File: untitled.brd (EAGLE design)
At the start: 59.4 x 57.8 mm, 21 parts

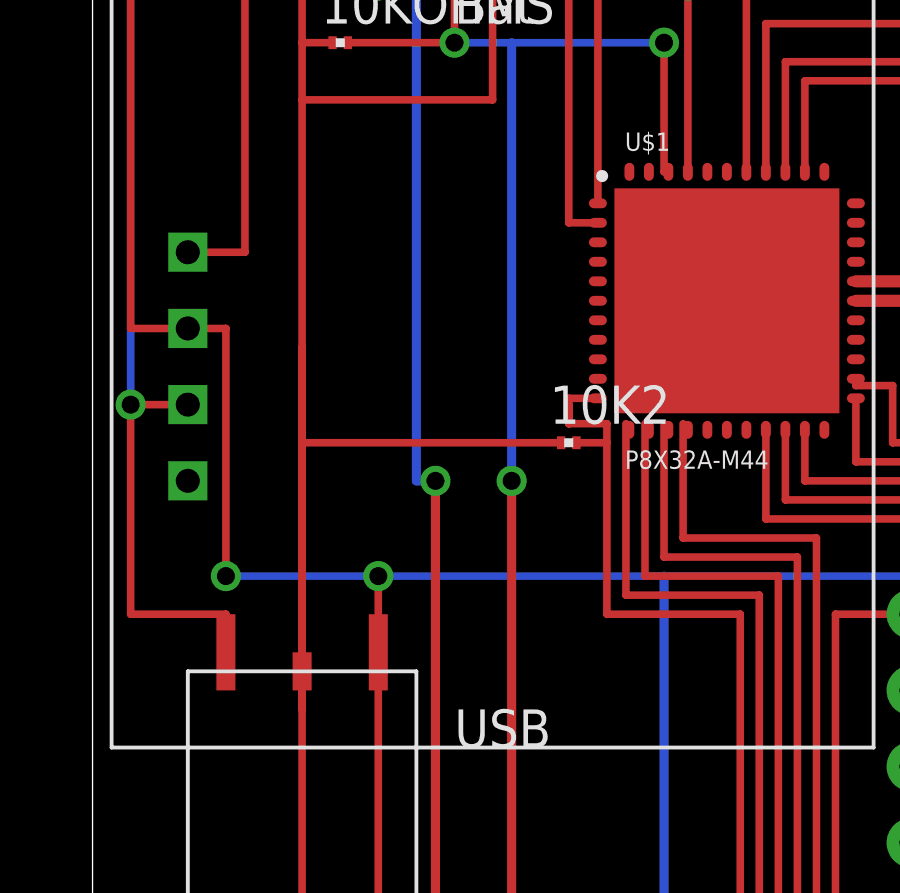
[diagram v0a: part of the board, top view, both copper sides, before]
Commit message: added power pins
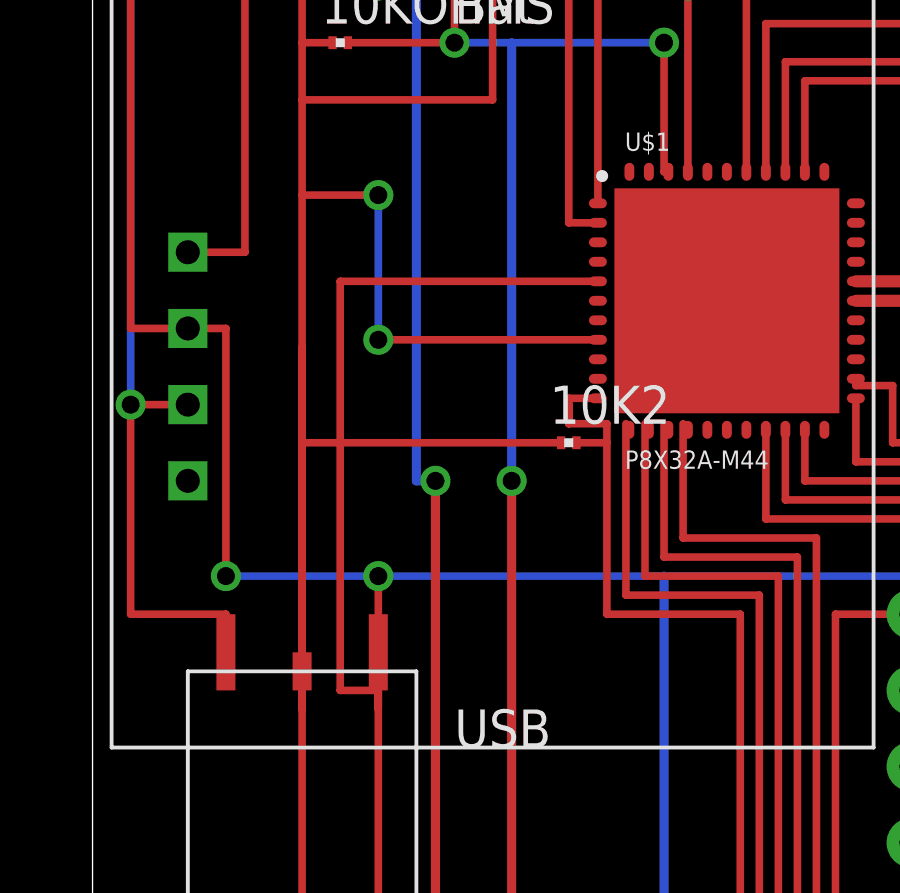
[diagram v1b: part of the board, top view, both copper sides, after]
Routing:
- net VSS: track 0.00 -> 24.1 mm
- net VDD: track 0.00 -> 14.7 mm, vias 0 -> 2
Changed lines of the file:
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@@
 <contactref element="U$1" pad="30"/>
 <contactref element="U$1" pad="40"/>
-<wire x1="55.45" y1="38.5313" x2="50.5" y2="41.5313" width="0" layer="19" extent="1-1"/>
 <wire x1="59.1" y1="44.1313" x2="55.45" y2="38.5313" width="0" layer="19" extent="1-1"/>
 <wire x1="54.15" y1="47.1313" x2="59.1" y2="44.1313" width="0" layer="19" extent="1-1"/>
+<wire x1="50.5" y1="41.5313" x2="43.18" y2="41.5313" width="0.254" layer="1"/>
+<wire x1="43.18" y1="41.5313" x2="43.18" y2="46.355" width="0.254" layer="16"/>
+<wire x1="43.18" y1="46.355" x2="40.64" y2="46.355" width="0.254" layer="1"/>
+<wire x1="40.64" y1="46.355" x2="54.15" y2="47.1313" width="0" layer="19" extent="1-16"/>
+<via x="43.18" y="41.5313" extent="1-16" drill="0.6" shape="square"/>
+<via x="43.18" y="46.355" extent="1-16" drill="0.6" shape="square"/>
 </signal>
 <signal name="VSS">
@@
 <contactref element="U$1" pad="27"/>
 <contactref element="U$1" pad="39"/>
-<wire x1="54.8" y1="47.1313" x2="50.5" y2="43.4813" width="0" layer="19" extent="1-1"/>
 <wire x1="54.8" y1="38.5313" x2="50.5" y2="43.4813" width="0" layer="19" extent="1-1"/>
 <wire x1="59.1" y1="42.1813" x2="54.8" y2="38.5313" width="0" layer="19" extent="1-1"/>
+<wire x1="50.5" y1="43.4813" x2="41.91" y2="43.4813" width="0.254" layer="1"/>
+<wire x1="41.91" y1="43.4813" x2="41.91" y2="29.845" width="0.254" layer="1"/>
+<wire x1="41.91" y1="29.845" x2="43.18" y2="29.845" width="0.254" layer="1"/>
+<wire x1="43.18" y1="29.845" x2="43.18" y2="29.21" width="0.254" layer="1"/>
+<wire x1="43.18" y1="29.21" x2="54.8" y2="38.5313" width="0" layer="19" extent="1-16"/>
 </signal>
 <signal name="VBAT">

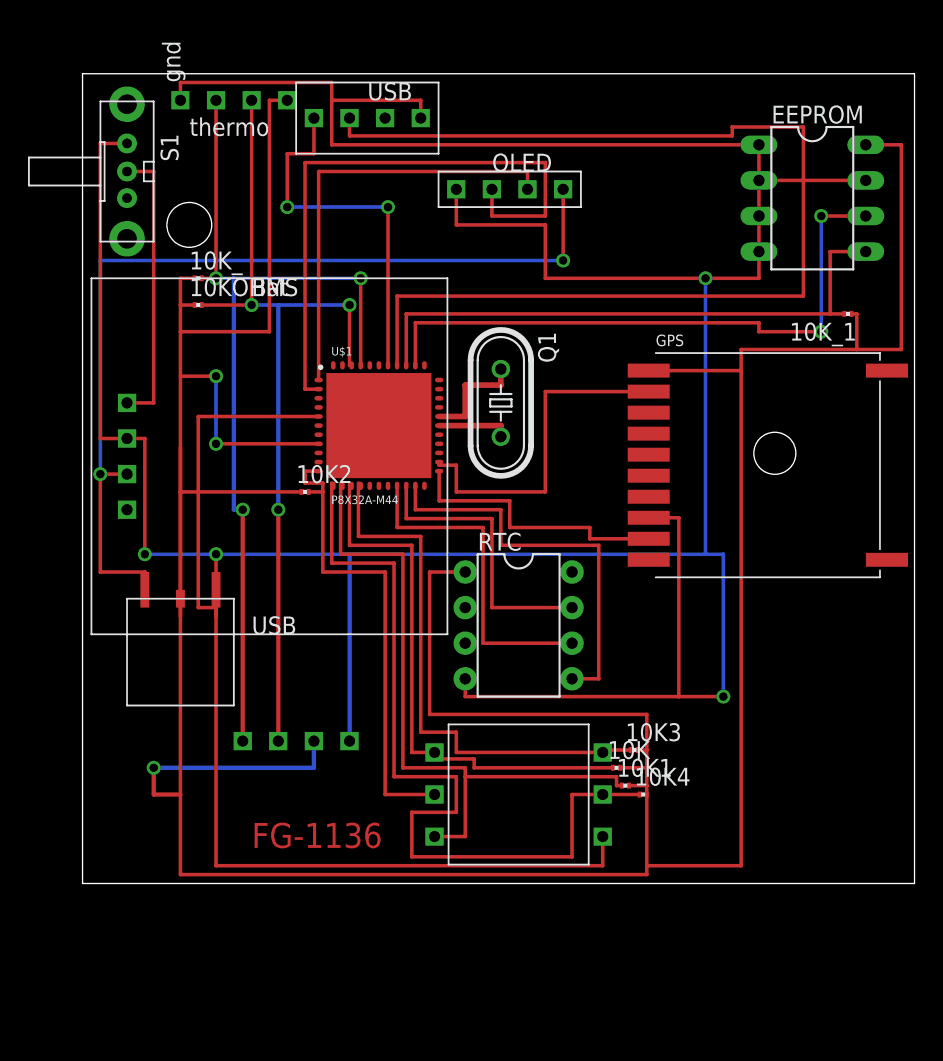
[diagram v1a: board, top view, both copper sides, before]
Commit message: used sane resistors
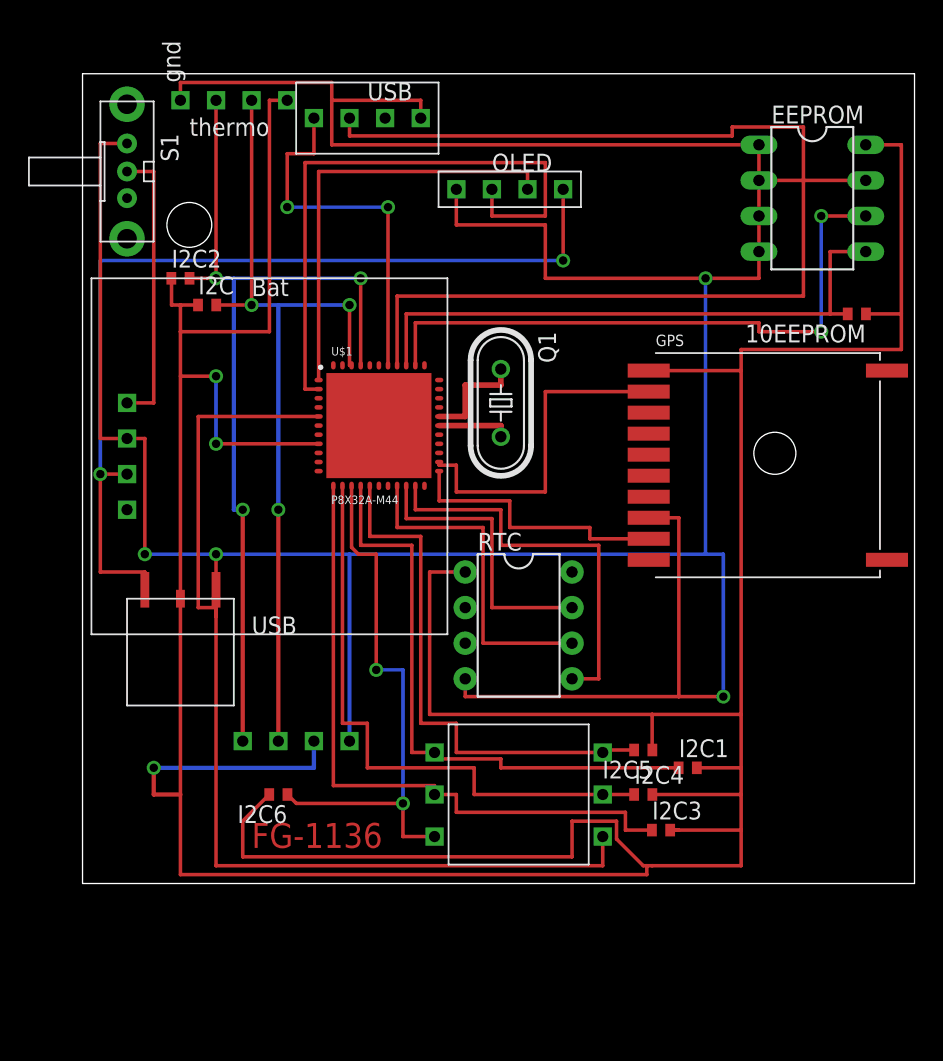
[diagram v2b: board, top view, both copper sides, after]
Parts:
- removed 10K, 10K1, 10K2, 10K3, 10K4, 10KOHMS, 10K_, 10K_1: (no value), rcl:R0201
- added 10EEPROM, I2C, I2C1, I2C2, I2C3, I2C4, I2C5, I2C6: (no value), adafruit:R1005
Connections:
- removed net N$22: 10K2.1, 5WAYSWITCH.U
- removed net N$23: 10K3.1, 5WAYSWITCH.BTN
- removed net N$24: 10K4.1, 5WAYSWITCH.R
- new net N$14: 5WAYSWITCH.U, I2C1.1, U$1.15
- new net N$15: 5WAYSWITCH.D, I2C6.1, U$1.14
- new net N$17: 5WAYSWITCH.L, I2C3.1, U$1.12
- net N$18: now also 10EEPROM.2; no longer 10K_1.2
- net N$20: now also 5WAYSWITCH.R, I2C4.1, U$1.13; no longer 10K.1, 5WAYSWITCH.D
- net N$21: now also 5WAYSWITCH.BTN, I2C5.2, U$1.16; no longer 10K1.1, 5WAYSWITCH.L
- net SCL: now also I2C2.2; no longer 10K_.2
- net SDA: now also I2C.2; no longer 10KOHMS.2
- net VCC: now also 10EEPROM.1, I2C.1, I2C1.2, I2C2.1, I2C3.2, I2C4.2, I2C5.1, I2C6.2; no longer 10K.2, 10K1.2, 10K2.2, 10K3.2, 10K4.2, 10KOHMS.1, 10K_.1, 10K_1.1, U$1.11, U$1.12, U$1.13, U$1.14, U$1.15
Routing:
- net N$24: track 59.4 -> 0.00 mm
- net N$17: track 0.00 -> 47.3 mm
- net N$22: track 46.0 -> 0.00 mm
- net VCC: track 247.0 -> 291.6 mm
- net N$14: track 0.00 -> 42.8 mm
- net N$15: track 0.00 -> 39.2 mm, vias 0 -> 2
- net N$23: track 38.8 -> 0.00 mm
- net N$20: track 50.7 -> 42.8 mm
- net N$21: track 43.9 -> 38.1 mm
- net SDA: track 60.7 -> 59.7 mm
- net SCL: track 63.9 -> 64.8 mm
- net N$16: track 0.00 -> 0.64 mm

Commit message: replaced compass break out with raw part
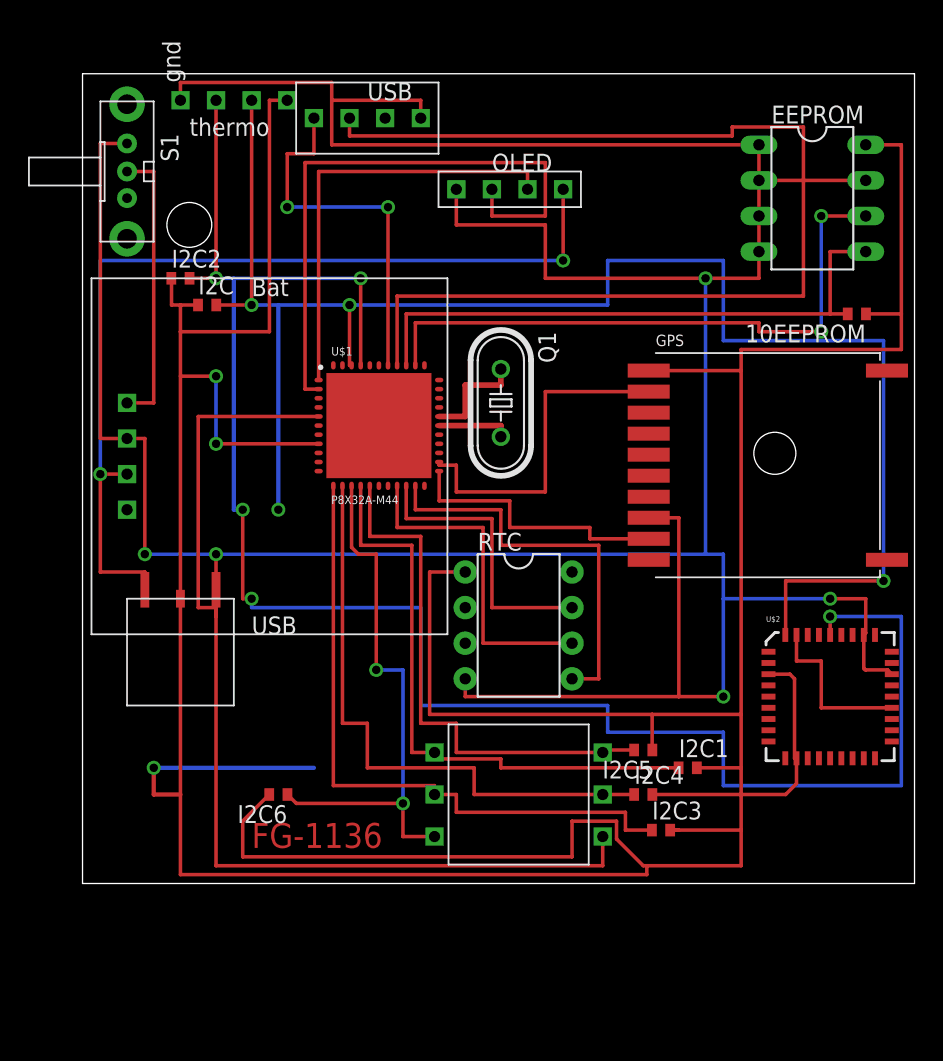
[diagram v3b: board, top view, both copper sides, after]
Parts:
- removed COMPASS: HMC6343, HMC6343Board:HMC6343
- added U$2: HMC6343A, SparkFun:LCC36
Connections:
- new net N$22: U$2.22, U$2.35
- net GND: now also U$2.25, U$2.29; no longer COMPASS.GND
- net SCL: now also U$2.32; no longer COMPASS.SCL
- net SDA: now also U$2.36; no longer COMPASS.SDA
- net VCC: now also U$2.11, U$2.3; no longer COMPASS.VCC
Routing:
- net SCL: track 64.8 -> 133.4 mm, vias 3 -> 5
- net SDA: track 59.7 -> 118.2 mm, vias 3 -> 4
- net N$22: track 0.00 -> 12.0 mm
- net VCC: track 291.6 -> 303.6 mm
- net GND: track 305.0 -> 309.0 mm, vias 4 -> 5
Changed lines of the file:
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@@
 <element name="3.3LDO" library="ldo1117-33" package="1117-33" value="LDO1117-33" x="40.64" y="26.67" rot="R180"/>
 <element name="5WAYSWITCH" library="5-wayswitch" package="5-WAYSWITCH" value="5-WAYSWITCH" x="64.77" y="16.51"/>
-<element name="COMPASS" library="HMC6343Board" package="HMC6343" value="HMC6343" x="47.625" y="22.86" rot="MR270"/>
 <element name="EEPROM" library="adafruit" package="DIL08" value="DS1307" x="85.725" y="59.055" rot="R270"/>
 <element name="GPS" library="adafruit" package="FGPMMOPA6B" value="" x="82.55" y="40.005"/>
@@
 <element name="I2C6" library="adafruit" package="R1005" value="" x="47.625" y="16.51" rot="R180"/>
 <element name="I2C1" library="adafruit" package="R1005" value="" x="76.835" y="18.415"/>
+<element name="U$2" library="SparkFun" package="LCC36" value="HMC6343A" x="86.995" y="23.495"/>
 </elements>
 <signals>
@@
 <wire x1="80.645" y1="16.51" x2="80.645" y2="13.97" width="0.254" layer="1"/>
 <wire x1="80.645" y1="13.97" x2="80.645" y2="11.43" width="0.254" layer="1"/>
-<wire x1="80.645" y1="11.43" x2="74.295" y2="11.43" width="0.254" layer="1"/>
-<wire x1="74.295" y1="11.43" x2="73.915" y2="11.43" width="0.254" layer="1"/>
+<wire x1="80.645" y1="11.43" x2="73.915" y2="11.43" width="0.254" layer="1"/>
 <wire x1="80.645" y1="48.26" x2="92.075" y2="48.26" width="0.254" layer="1"/>
 <wire x1="89.535" y1="62.865" x2="92.075" y2="62.865" width="0.254" layer="1"/>
@@
 <wire x1="46.99" y1="66.04" x2="46.99" y2="49.53" width="0.254" layer="1"/>
 <wire x1="46.99" y1="49.53" x2="40.64" y2="49.53" width="0.254" layer="1"/>
-<contactref element="COMPASS" pad="VCC"/>
-<wire x1="50.165" y1="20.32" x2="50.165" y2="18.415" width="0.3048" layer="16"/>
 <wire x1="50.165" y1="18.415" x2="38.735" y2="18.415" width="0.3048" layer="16"/>
 <via x="38.735" y="18.415" extent="1-16" drill="0.6" shape="square"/>
@@
 <wire x1="71.755" y1="13.335" x2="73.66" y2="11.43" width="0.254" layer="1"/>
 <wire x1="73.66" y1="11.43" x2="73.915" y2="11.43" width="0.254" layer="1"/>
+<contactref element="U$2" pad="3"/>
+<contactref element="U$2" pad="11"/>
+<wire x1="84.595" y1="19.095" x2="84.455" y2="19.095" width="0.254" layer="1"/>
+<wire x1="84.455" y1="19.095" x2="84.455" y2="24.765" width="0.254" layer="1"/>
+<wire x1="82.595" y1="25.095" x2="84.125" y2="25.095" width="0.254" layer="1"/>
+<wire x1="84.125" y1="25.095" x2="84.455" y2="24.765" width="0.254" layer="1"/>
+<wire x1="84.595" y1="19.095" x2="84.595" y2="17.285" width="0.254" layer="1"/>
+<wire x1="84.595" y1="17.285" x2="83.82" y2="16.51" width="0.254" layer="1"/>
+<wire x1="83.82" y1="16.51" x2="80.645" y2="16.51" width="0.254" layer="1"/>
 </signal>
 <signal name="N$1">
@@
 </signal>
 <signal name="GND">
-<contactref element="COMPASS" pad="GND"/>
 <contactref element="RTC" pad="4"/>
 <contactref element="THERMO" pad="GND"/>
@@
 <wire x1="70.77" y1="11.43" x2="70.77" y2="13.51" width="0.254" layer="1"/>
 <wire x1="43.18" y1="31.75" x2="43.18" y2="33.655" width="0.254" layer="1"/>
-<wire x1="43.18" y1="33.655" x2="52.705" y2="33.655" width="0.254" layer="16"/>
-<wire x1="52.705" y1="33.655" x2="78.105" y2="33.655" width="0.254" layer="16"/>
+<wire x1="43.18" y1="33.655" x2="78.105" y2="33.655" width="0.254" layer="16"/>
 <wire x1="78.105" y1="33.655" x2="79.375" y2="33.655" width="0.254" layer="16"/>
-<wire x1="79.375" y1="33.655" x2="79.375" y2="23.495" width="0.254" layer="16"/>
+<wire x1="79.375" y1="33.655" x2="79.375" y2="30.48" width="0.254" layer="16"/>
+<wire x1="79.375" y1="30.48" x2="79.375" y2="23.495" width="0.254" layer="16"/>
 <wire x1="79.375" y1="23.495" x2="76.2" y2="23.495" width="0.254" layer="1"/>
 <wire x1="76.2" y1="23.495" x2="60.96" y2="23.495" width="0.254" layer="1"/>
@@
 <wire x1="74.05" y1="36.255" x2="76.2" y2="36.255" width="0.254" layer="1"/>
 <wire x1="76.2" y1="36.255" x2="76.2" y2="23.495" width="0.254" layer="1"/>
-<wire x1="52.705" y1="20.32" x2="52.705" y2="33.655" width="0.3048" layer="16"/>
+<contactref element="U$2" pad="29"/>
+<contactref element="U$2" pad="25"/>
+<wire x1="89.395" y1="27.895" x2="89.395" y2="25.54" width="0.254" layer="1"/>
+<wire x1="89.395" y1="25.54" x2="89.535" y2="25.4" width="0.254" layer="1" curve="90"/>
+<wire x1="89.535" y1="25.4" x2="91.09" y2="25.4" width="0.254" layer="1"/>
+<wire x1="91.09" y1="25.4" x2="91.395" y2="25.095" width="0.254" layer="1"/>
+<via x="86.995" y="30.48" extent="1-16" drill="0.6" shape="square"/>
+<wire x1="86.995" y1="30.48" x2="79.375" y2="30.48" width="0.254" layer="16"/>
+<wire x1="89.395" y1="27.895" x2="89.535" y2="28.035" width="0.254" layer="1"/>
+<wire x1="89.535" y1="28.035" x2="89.535" y2="30.48" width="0.254" layer="1"/>
 <wire x1="81.915" y1="60.325" x2="81.915" y2="57.785" width="0" layer="19" extent="1-1"/>
+<wire x1="89.535" y1="30.48" x2="86.995" y2="30.48" width="0.254" layer="1"/>
 </signal>
 <signal name="N$5">
@@
 <signal name="SCL">
 <contactref element="U$1" pad="41"/>
-<contactref element="COMPASS" pad="SCL"/>
 <contactref element="THERMO" pad="SCL"/>
 <wire x1="43.18" y1="53.34" x2="43.18" y2="66.04" width="0.254" layer="1"/>
@@
 <via x="43.18" y="53.34" extent="1-16" drill="0.6" shape="octagon"/>
 <via x="53.5" y="53.34" extent="1-16" drill="0.6" shape="octagon"/>
-<wire x1="45.085" y1="20.32" x2="45.085" y2="36.83" width="0.3048" layer="1"/>
 <via x="45.085" y="36.83" extent="1-16" drill="0.6" shape="square"/>
 <wire x1="45.085" y1="36.83" x2="44.45" y2="36.83" width="0.3048" layer="16"/>
@@
 <contactref element="I2C2" pad="2"/>
 <wire x1="41.29" y1="53.34" x2="43.18" y2="53.34" width="0.254" layer="1"/>
+<contactref element="U$2" pad="32"/>
+<wire x1="86.995" y1="27.895" x2="86.995" y2="29.21" width="0.254" layer="1"/>
+<via x="86.995" y="29.21" extent="1-16" drill="0.6" shape="square"/>
+<wire x1="86.995" y1="29.21" x2="92.075" y2="29.21" width="0.254" layer="16"/>
+<wire x1="92.075" y1="29.21" x2="92.075" y2="17.145" width="0.254" layer="16"/>
+<wire x1="92.075" y1="17.145" x2="79.375" y2="17.145" width="0.254" layer="16"/>
+<wire x1="79.375" y1="17.145" x2="79.375" y2="20.955" width="0.254" layer="16"/>
+<wire x1="79.375" y1="20.955" x2="71.12" y2="20.955" width="0.254" layer="16"/>
+<wire x1="71.12" y1="20.955" x2="71.12" y2="22.86" width="0.254" layer="16"/>
+<wire x1="71.12" y1="22.86" x2="57.785" y2="22.86" width="0.254" layer="16"/>
+<wire x1="57.785" y1="22.86" x2="57.785" y2="29.845" width="0.254" layer="16"/>
+<wire x1="57.785" y1="29.845" x2="45.72" y2="29.845" width="0.254" layer="16"/>
+<wire x1="45.72" y1="29.845" x2="45.72" y2="30.48" width="0.254" layer="16"/>
+<via x="45.72" y="30.48" extent="1-16" drill="0.6" shape="square"/>
+<wire x1="45.72" y1="30.48" x2="45.085" y2="30.48" width="0.254" layer="1"/>
+<wire x1="45.085" y1="30.48" x2="45.085" y2="36.83" width="0.254" layer="1"/>
 </signal>
 <signal name="SDA">
-<contactref element="COMPASS" pad="SDA"/>
 <contactref element="THERMO" pad="SDA"/>
 <contactref element="U$1" pad="42"/>
@@
 <wire x1="52.705" y1="51.435" x2="47.625" y2="51.435" width="0.254" layer="16"/>
 <wire x1="47.625" y1="51.435" x2="45.72" y2="51.435" width="0.254" layer="16"/>
-<wire x1="47.625" y1="20.32" x2="47.625" y2="36.83" width="0.3048" layer="1"/>
 <via x="47.625" y="36.83" extent="1-16" drill="0.6" shape="square"/>
 <wire x1="47.625" y1="36.83" x2="47.625" y2="51.435" width="0.3048" layer="16"/>
 <contactref element="I2C" pad="2"/>
 <wire x1="43.195" y1="51.435" x2="45.72" y2="51.435" width="0.254" layer="1"/>
+<contactref element="U$2" pad="36"/>
+<wire x1="83.795" y1="27.895" x2="83.82" y2="27.92" width="0.254" layer="1"/>
+<wire x1="83.82" y1="27.92" x2="83.82" y2="31.75" width="0.254" layer="1"/>
+<wire x1="83.82" y1="31.75" x2="90.805" y2="31.75" width="0.254" layer="1"/>
+<via x="90.805" y="31.75" extent="1-16" drill="0.6" shape="square"/>
+<wire x1="90.805" y1="31.75" x2="90.805" y2="48.895" width="0.254" layer="16"/>
+<wire x1="90.805" y1="48.895" x2="79.375" y2="48.895" width="0.254" layer="16"/>
+<wire x1="79.375" y1="48.895" x2="79.375" y2="54.61" width="0.254" layer="16"/>
+<wire x1="79.375" y1="54.61" x2="71.12" y2="54.61" width="0.254" layer="16"/>
+<wire x1="71.12" y1="54.61" x2="71.12" y2="51.435" width="0.254" layer="16"/>
+<wire x1="71.12" y1="51.435" x2="52.705" y2="51.435" width="0.254" layer="16"/>
 </signal>
 <signal name="N$3">
@@
 <wire x1="54.15" y1="34.925" x2="54.15" y2="38.5313" width="0.254" layer="1"/>
 </signal>
+<signal name="N$22">
+<contactref element="U$2" pad="22"/>
+<contactref element="U$2" pad="35"/>
+<wire x1="91.395" y1="22.695" x2="86.36" y2="22.695" width="0.254" layer="1"/>
+<wire x1="86.36" y1="22.695" x2="86.36" y2="26.035" width="0.254" layer="1"/>
+<wire x1="86.36" y1="26.035" x2="84.595" y2="26.035" width="0.254" layer="1"/>
+<wire x1="84.595" y1="26.035" x2="84.595" y2="27.895" width="0.254" layer="1"/>
+</signal>
 </signals>

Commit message: Add missing junctions to schematic
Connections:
- net VCC: now also U$2.21
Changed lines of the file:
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@@
 <wire x1="84.595" y1="17.285" x2="83.82" y2="16.51" width="0.254" layer="1"/>
 <wire x1="83.82" y1="16.51" x2="80.645" y2="16.51" width="0.254" layer="1"/>
+<contactref element="U$2" pad="21"/>
+<wire x1="84.595" y1="19.095" x2="91.395" y2="21.895" width="0" layer="19" extent="1-1"/>
 </signal>
 <signal name="N$1">
